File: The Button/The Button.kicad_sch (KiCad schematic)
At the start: 28 parts, among them J1 Gnd, J2 2169890001, J3 Extra Pins, J4 Buttons, J5 Conn_01x05_Pin, SW8 SW_SPST BOOT, U1 LD1117S33TR_SOT223, U2 STM32C071KBTx, U5 USBLC6-2SC6

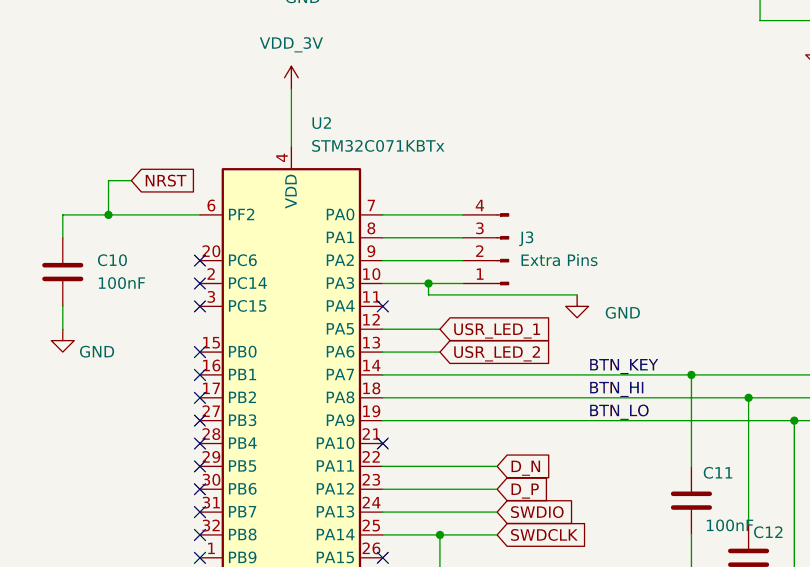
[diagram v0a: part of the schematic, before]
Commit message: Move character conversion to separate file
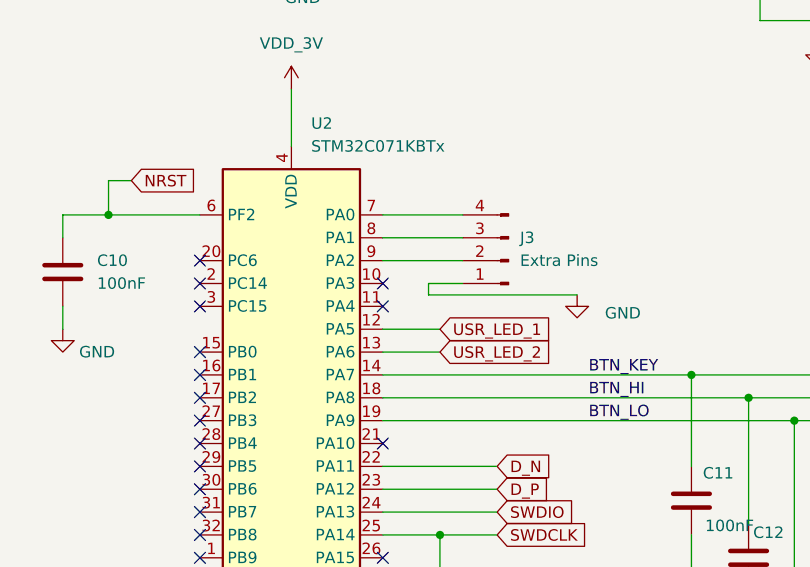
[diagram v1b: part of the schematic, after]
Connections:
- net GND: no longer U2.10 (PA3)
- no-connect marks 17 -> 18
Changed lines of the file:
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@@
-	)
-	(junction
-		(at 218.44 81.28)
-		(diameter 0)
-		(color 0 0 0 0)
 	)
 	(junction
@@
 	)
 	(no_connect
+		(at 213.36 81.28)
+	)
+	(no_connect
 		(at 193.04 83.82)
 	)
@@
 		)
 		(stroke
-			(width 0)
-			(type default)
-		)
-	)
-	(wire
-		(pts
-			(xy 213.36 81.28) (xy 218.44 81.28)
-		)
-		(stroke
